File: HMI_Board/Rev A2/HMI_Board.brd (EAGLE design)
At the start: 138 x 34.4 mm, 35 parts, among them SW1 B3FS-1015, SW2 B3FS-1015, SW3 B3FS-1015, SW4 B3FS-1015, SW5 B3FS-1015, SW6 B3FS-1015, U1 90814-0208, U2 90814-0206

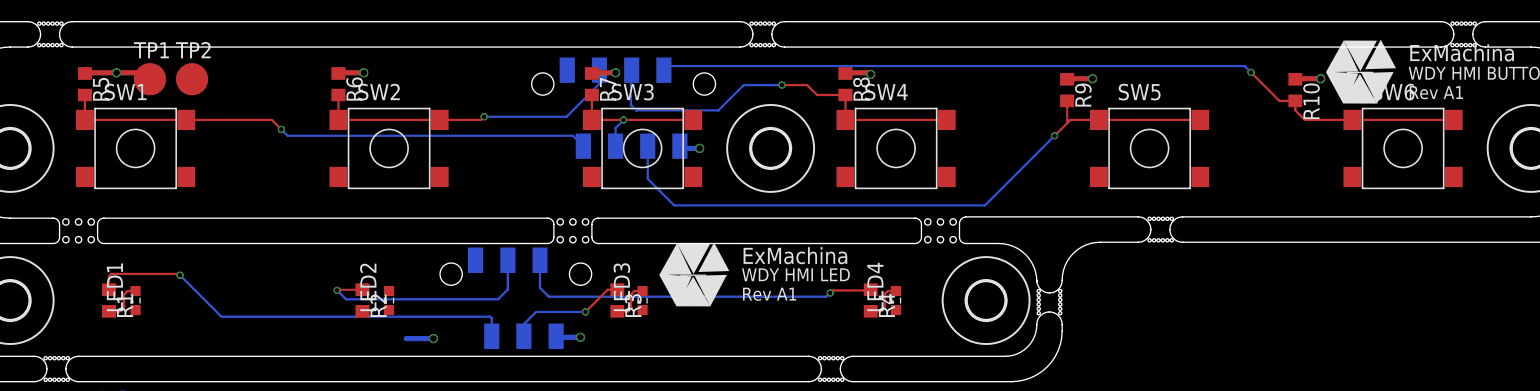
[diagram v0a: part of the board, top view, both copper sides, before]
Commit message: Adjust the position of the component
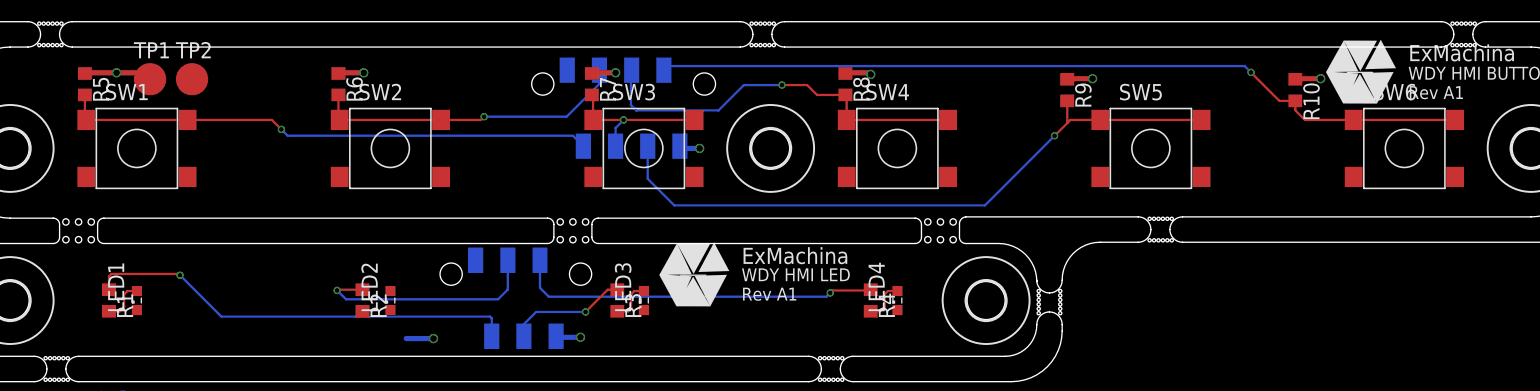
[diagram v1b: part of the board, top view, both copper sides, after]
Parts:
- moved LED1 0.10 mm to (19.0, 9.40)
- moved LED2 0.10 mm to (39.0, 9.40)
- moved LED3 0.10 mm to (59.0, 9.40)
- moved SW1 0.10 mm to (19.0, 21.4)
- moved SW2 0.10 mm to (39.0, 21.4)
- moved SW3 0.10 mm to (59.0, 21.4)
- moved LED4 0.10 mm to (79.0, 9.40)
- moved SW4 0.10 mm to (79.0, 21.4)
- moved SW5 0.10 mm to (99.0, 21.4)
- moved SW6 0.10 mm to (119.0, 21.4)

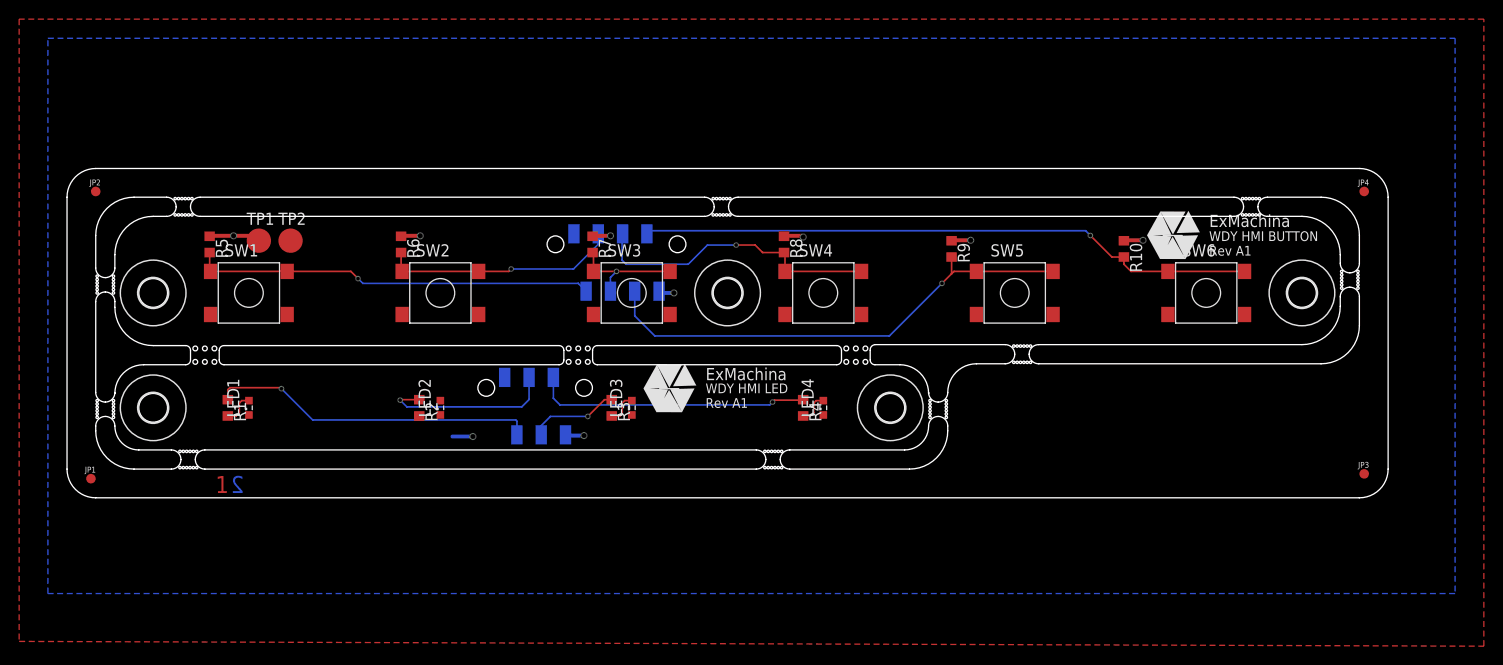
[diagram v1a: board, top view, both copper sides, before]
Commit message: Add MDP folder to HMI Board rev A2
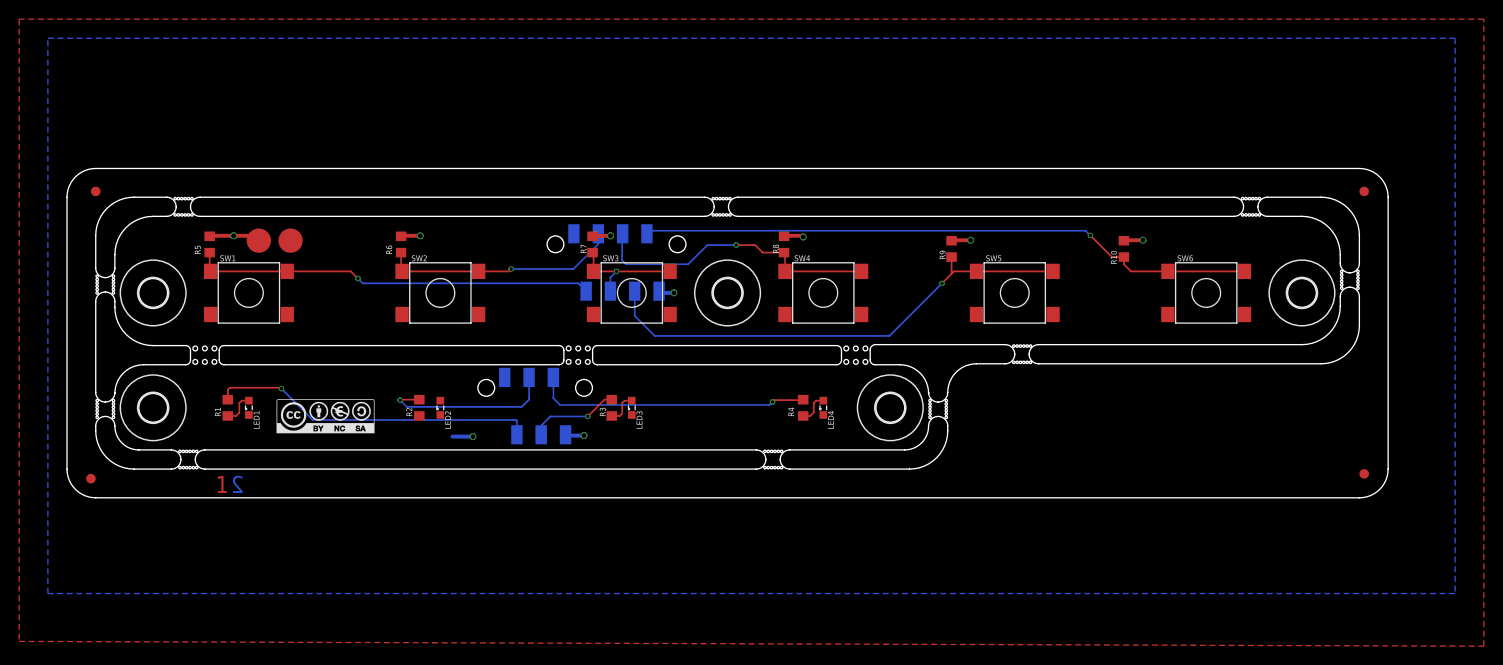
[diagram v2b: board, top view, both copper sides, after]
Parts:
- removed U$1: EXMACHINA-LOGO-NAME, exmachina:EXM-LOGO-BASELINE
- added T1: EXMACHINA-LOGO-NAME, exmachina:EXM-LOGO-BASELINE
- added U$3, U$4: (no value), cc-by-sa:CC-BY-NC-SA
- moved H4 77.0 mm to (9.00, 9.40)
- moved H3 61.2 mm to (69.0, 21.4)
- moved U$2 23.0 mm to (92.5, 25.9), flipped to the bottom
- moved H2 20.8 mm to (86.0, 9.40)
- renumbered H6 to H5, U1 to J2, U2 to J1
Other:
- board text added: "WDY HMI BUTTON Rev A2"
- board text added: "WDY HMI LED Rev A2"
- board text removed: "WDY HMI BUTTON Rev A1"
- board text removed: "WDY HMI LED Rev A1"

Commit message: Correct panel and generate Gerber
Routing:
- net N$2: track 0.00 -> 3.45 mm
- net +3V3: track 15.7 -> 17.2 mm
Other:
- outline, holes or cut-outs redrawn
